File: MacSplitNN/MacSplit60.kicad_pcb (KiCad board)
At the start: 2 copper layers, 157.7 x 126.1 mm, 74 parts, among them J1 USB_C_Receptacle_USB2.0, SW1 SW_Push, SW10 SW_Push, SW100 SW_SPST, SW11 SW_Push, SW12 SW_Push, SW13 SW_Push, SW14 SW_Push, SW15 SW_Push, SW16 SW_Push, SW17 SW_Push, SW18 SW_Push, SW19 SW_Push, SW2 SW_Push, SW20 SW_Push, SW21 SW_Push, SW22 SW_Push, SW23 SW_Push, SW24 SW_Push, SW25 SW_Push, SW26 SW_Push, SW27 SW_Push, SW28 SW_Push, SW29 SW_Push, SW3 SW_Push, SW30 SW_Push, SW4 SW_Push, SW5 SW_Push, SW6 SW_Push, SW7 SW_Push, SW8 SW_Push, SW9 SW_Push, U1 Pico, U2 MCP23S17_ML

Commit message: Updates switches positions according to MacSplit60 layout
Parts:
- removed H1: MountingHole, MountingHole:MountingHole_2.7mm_M2.5
- SW29, SW30: footprint Switch_Keyboard_Kailh:SW_Kailh_Choc_V1V2_1.00u -> Switch_Keyboard_Kailh:SW_Kailh_Choc_V1V2_1.50u
- moved D33 146.1 mm to (92.2, 75.6), turned to 90.3142 degrees
- moved SW30 140.1 mm to (97.0, 75.5), turned to -90 degrees
- moved H2 38.0 mm to (244.1, 136.4)
- moved D32 10.7 mm to (234.5, 130.2), turned to 90.3142 degrees
- moved H6 8.60 mm to (107.5, 138.3)
- moved SW29 5.24 mm to (229.6, 130.3), turned to 90 degrees
- moved H3 0.70 mm to (248.2, 39.3)
- moved H4 0.21 mm to (97.8, 39.3)
- moved SW18 0.20 mm to (210.8, 99.0)
- moved H7 0.20 mm to (172.3, 39.3)
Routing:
- net /COL_3: track 37.4 -> 29.2 mm, vias 2 -> 1
- net /INTB: track 46.3 -> 39.2 mm
- net /~{RESET}: track 48.7 -> 42.3 mm
- net /ROW_2: track 23.1 -> 17.3 mm, vias 1 -> 0
- net /ROW_0: track 25.9 -> 21.1 mm, vias 1 -> 0
- net /COL_5: track 23.6 -> 19.5 mm, vias 1 -> 0
- net /COL_0: track 49.6 -> 46.2 mm
- net /ROW_4: track 28.6 -> 25.3 mm, vias 1 -> 0
- net /ROW_3: track 26.5 -> 24.0 mm
- net /INTA: track 63.8 -> 61.4 mm
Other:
- board size 157.7 x 126.1 mm -> 166.1 x 112 mm

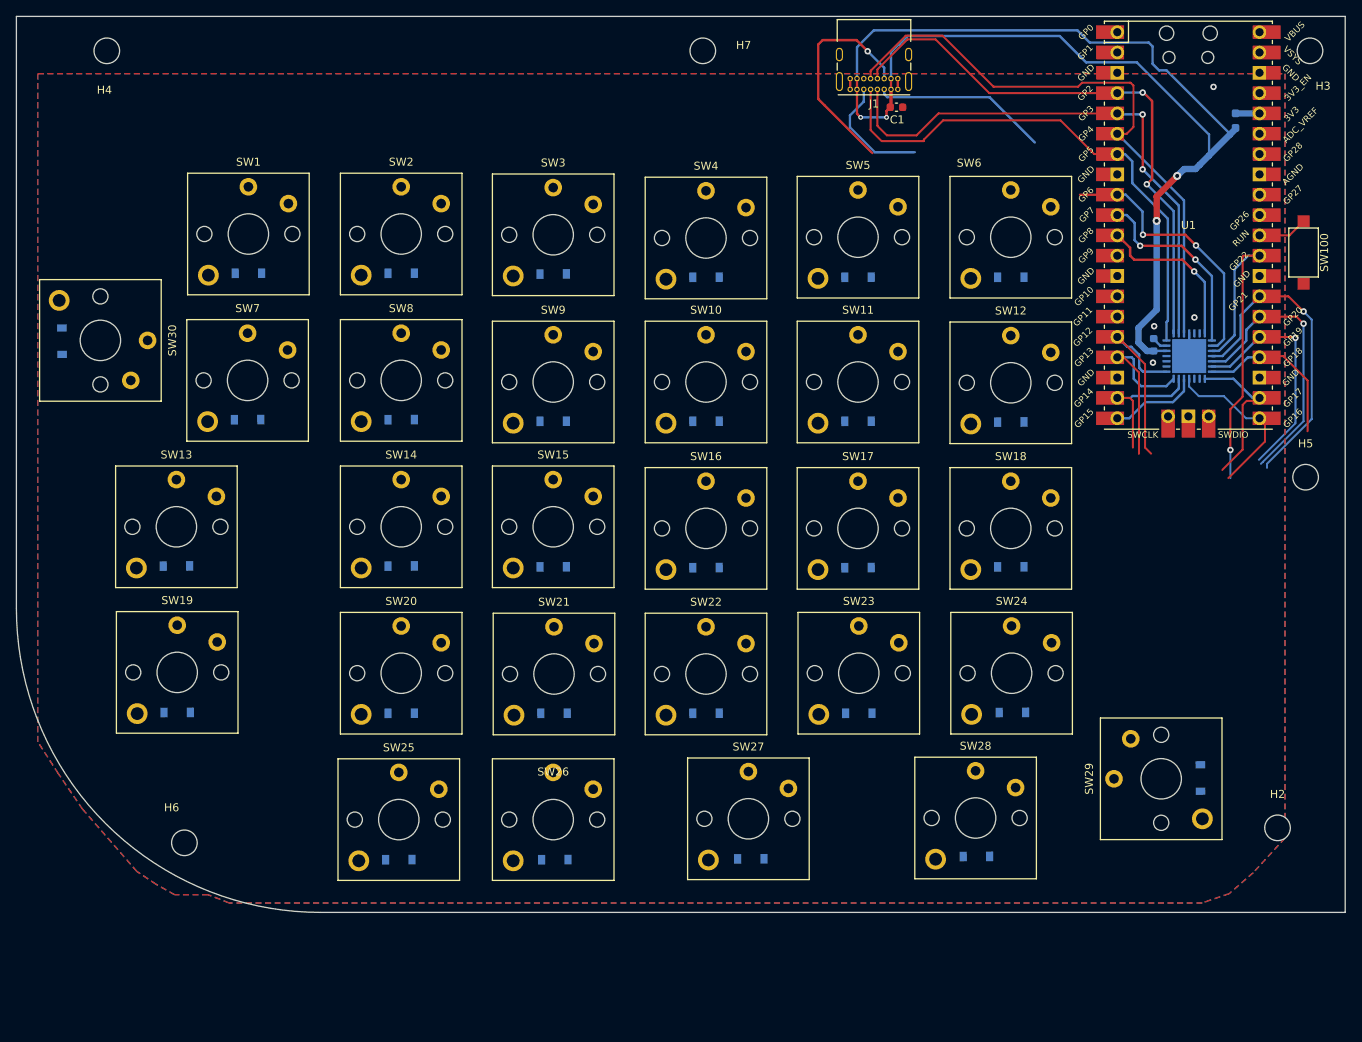
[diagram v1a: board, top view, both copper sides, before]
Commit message: Corrects the PCB edge
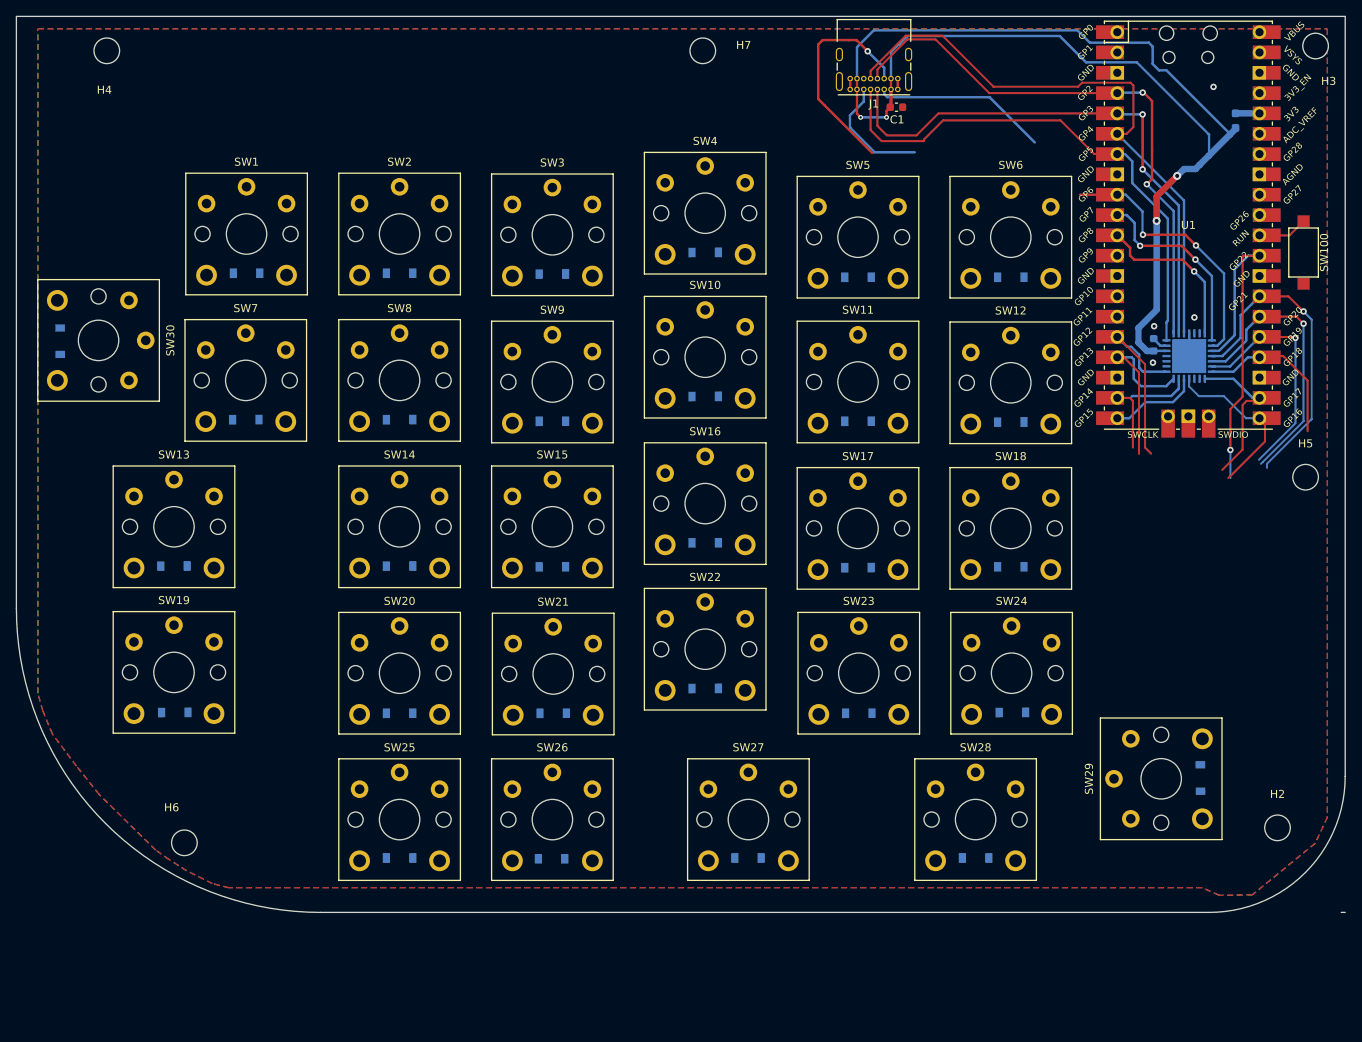
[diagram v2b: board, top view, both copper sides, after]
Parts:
- moved SW10 3.10 mm to (172.6, 77.6)
- moved SW22 3.10 mm to (172.6, 114.1)
- moved SW4 3.10 mm to (172.6, 59.6)
- moved D13 3.10 mm to (172.6, 82.5)
- moved D19 3.10 mm to (172.6, 100.8)
- moved D25 3.10 mm to (172.6, 119.0)
- moved D4 3.10 mm to (172.6, 64.5)
- moved SW16 3.10 mm to (172.6, 95.9)
- moved H3 0.92 mm to (248.9, 38.7)
- moved D29 0.41 mm to (153.4, 140.3), turned to 0 degrees
- moved SW19 0.40 mm to (106.2, 117.0)
- moved D30 0.37 mm to (177.9, 140.2), turned to 0 degrees
- moved D16 0.30 mm to (106.2, 103.7)
- moved D22 0.30 mm to (106.3, 122.0)
- moved SW13 0.30 mm to (106.2, 98.8)
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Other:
- outline, holes or cut-outs redrawn

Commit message: Equalises and checks switches spacing, diodes on both layers
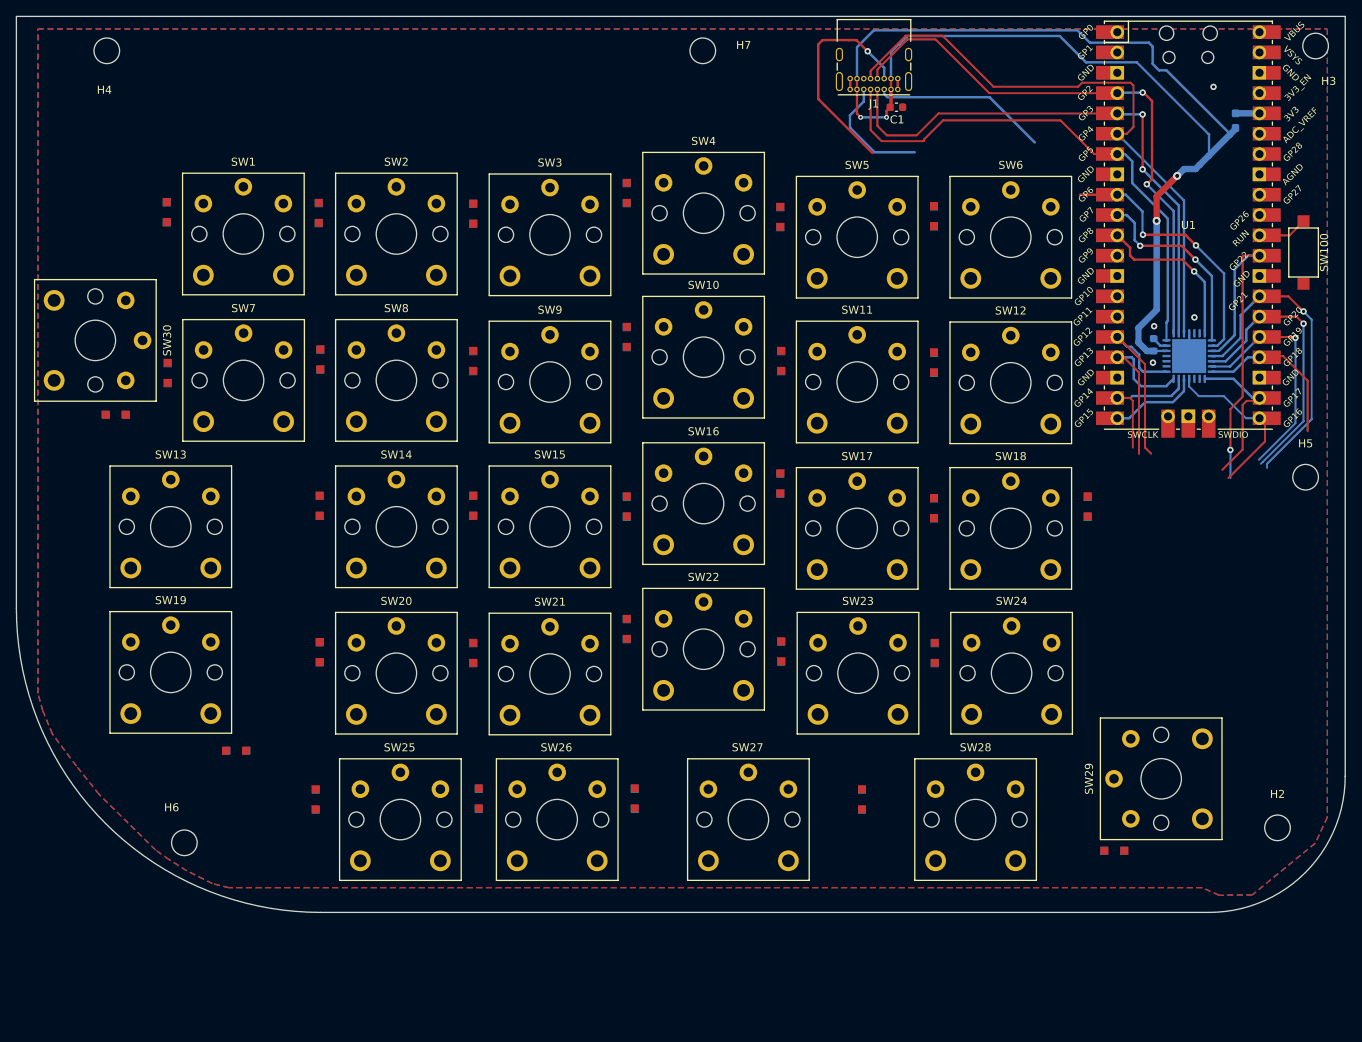
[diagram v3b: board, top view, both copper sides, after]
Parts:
- D1, D10, D11, D12, D13, D14, D15, D16, D17, D18, D19, D2, D20, D21, D22, D23, D24, D25, D26, D27, D28, D29, D3, D30, D31, D32, D33, D4, D5, D6: footprint Diode_SMD:D_SOD-123 -> Diode_SMD:D_SOD-323_Hand_Split_Keyboard
- moved D16 19.7 mm to (124.4, 96.2), turned to 90 degrees
- moved D30 16.0 mm to (163.8, 132.8), turned to 90 degrees
- moved D31 16.0 mm to (192.2, 132.9), turned to 90 degrees
- moved D32 14.1 mm to (223.7, 139.3), turned to 0 degrees
- moved D28 12.8 mm to (123.9, 132.9), turned to 90 degrees
- moved D2 12.6 mm to (124.3, 59.6), turned to 90 degrees
- moved D23 12.6 mm to (124.4, 114.5), turned to 90 degrees
- moved D1 12.5 mm to (105.3, 59.5), turned to 90 degrees
- moved D24 12.5 mm to (143.6, 114.6), turned to 90 degrees
- moved D12 12.4 mm to (143.6, 78.1), turned to 90 degrees
- moved D11 12.4 mm to (124.5, 77.9), turned to 90 degrees
- moved D3 12.4 mm to (143.6, 59.7), turned to 90 degrees
- moved D26 12.4 mm to (182.1, 114.4), turned to 90 degrees
- moved D13 12.3 mm to (162.8, 75.1), turned to 90 degrees
- moved D25 12.3 mm to (162.8, 111.6), turned to 90 degrees
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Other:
- outline, holes or cut-outs redrawn
- board text added: "LEFT"
- board text added: "RIGHT"

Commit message: Completes routing of the PCB
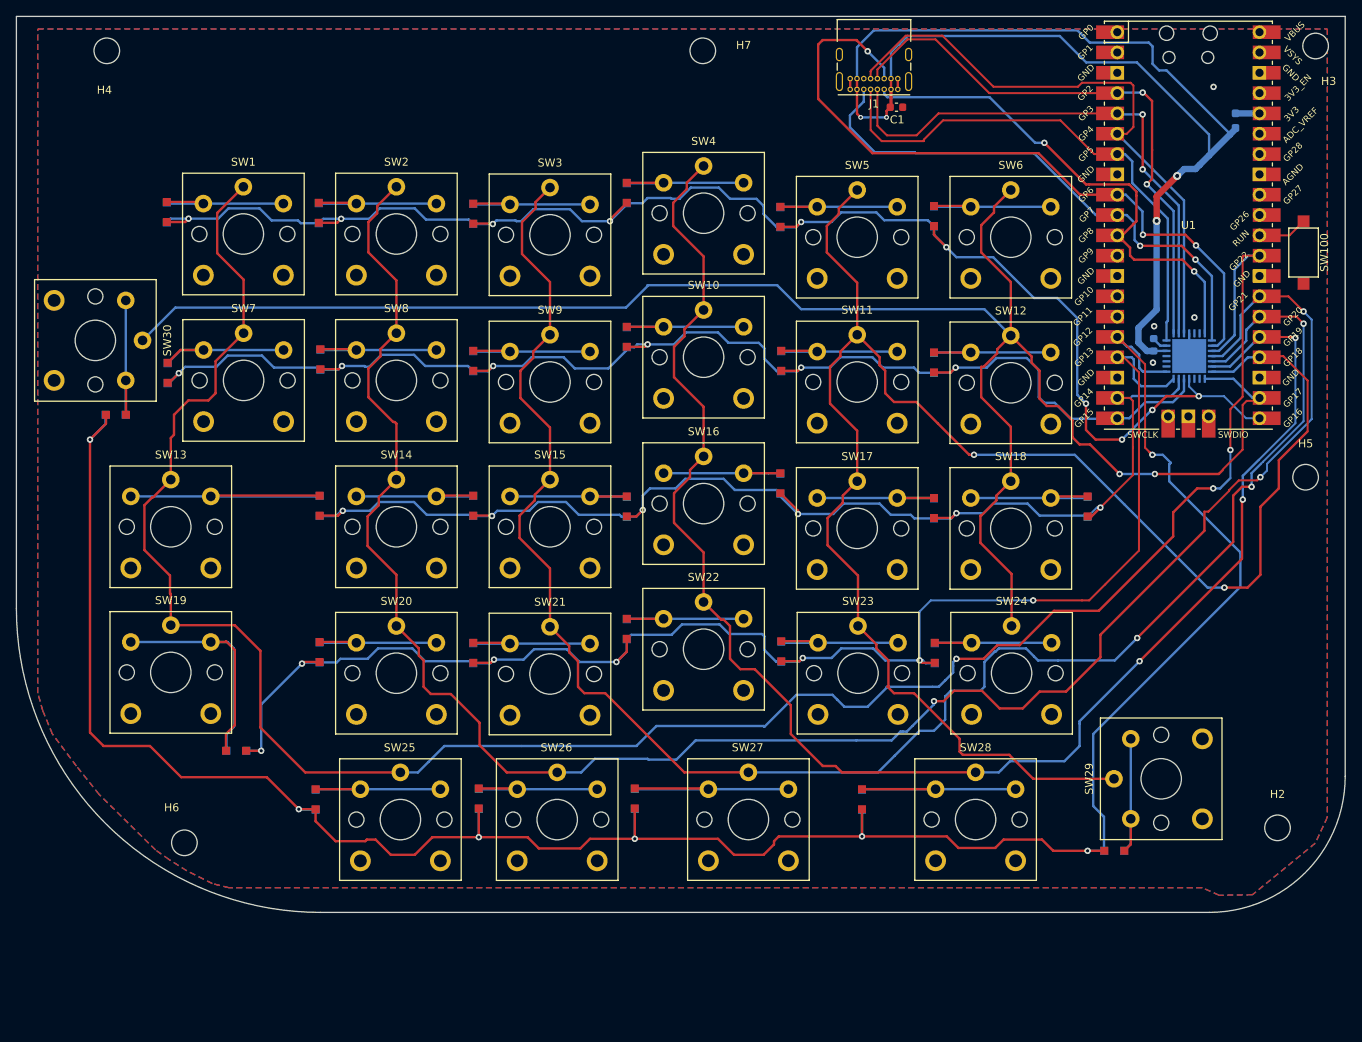
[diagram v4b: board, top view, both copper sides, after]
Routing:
- net /ROW_4: track 25.3 -> 298.9 mm, vias 0 -> 7
- net /COL_0: track 46.2 -> 276.6 mm, vias 1 -> 3
- net /COL_5: track 19.5 -> 235.1 mm, vias 0 -> 2
- net /COL_1: track 39.3 -> 244.8 mm, vias 1 -> 3
- net /COL_4: track 20.4 -> 213.9 mm, vias 0 -> 2
- net /COL_2: track 34.7 -> 222.6 mm, vias 1 -> 3
- net /COL_3: track 29.2 -> 199.7 mm, vias 1 -> 3
- net /ROW_0: track 21.1 -> 190.1 mm, vias 0 -> 10
- net /ROW_3: track 24.0 -> 192.2 mm, vias 0 -> 7
- net /ROW_1: track 11.3 -> 163.3 mm, vias 0 -> 6
- net /ROW_2: track 17.3 -> 151.2 mm, vias 0 -> 6
- net Net-(D22-Pad2): track 0.00 -> 43.0 mm
- net Net-(D16-Pad2): track 0.00 -> 37.3 mm
- net /INTB: track 39.2 -> 67.7 mm
- net Net-(D30-Pad2): track 0.00 -> 28.5 mm
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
